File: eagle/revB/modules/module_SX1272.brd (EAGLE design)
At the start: 24.1 x 32.8 mm, 18 parts, among them X1 734120110

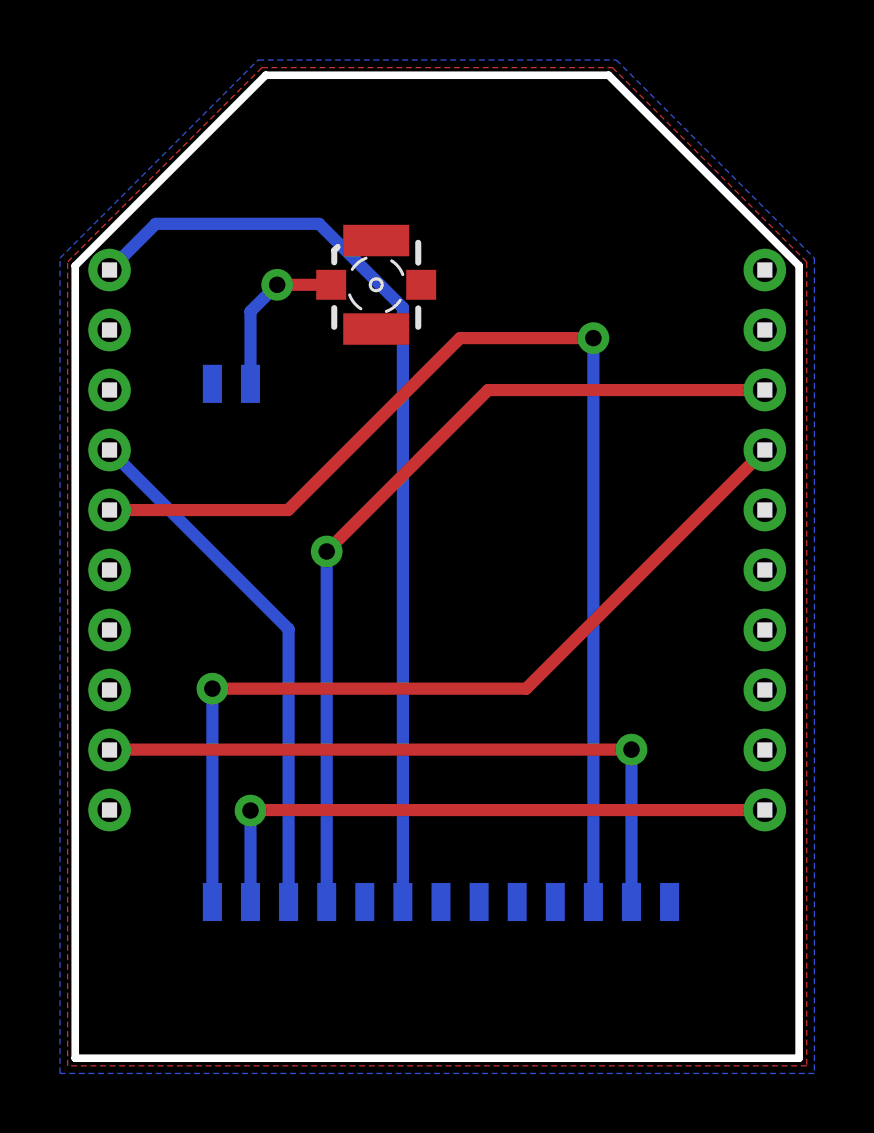
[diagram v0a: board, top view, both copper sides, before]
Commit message: Updated SX1272 layout
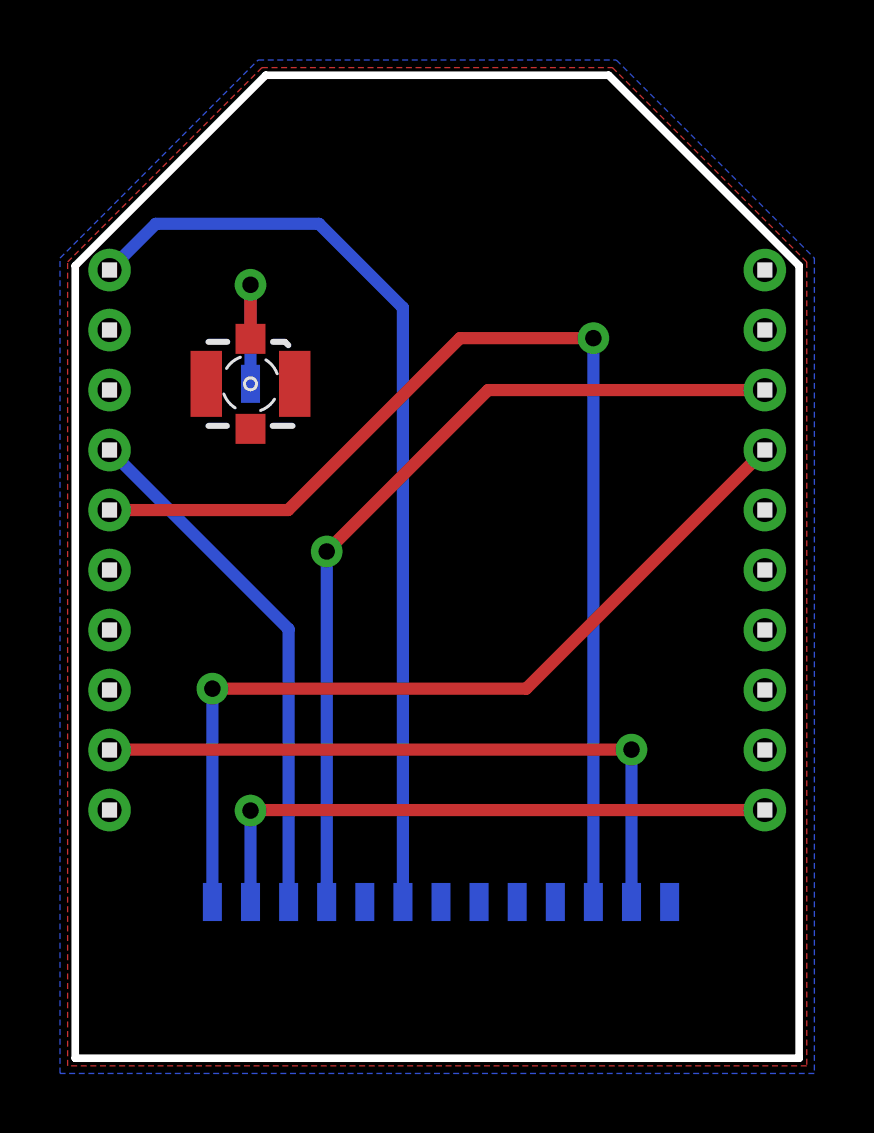
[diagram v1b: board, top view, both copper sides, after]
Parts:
- moved X1 5.34 mm to (5.97, 22.6), turned to 180 degrees
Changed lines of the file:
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@@
 <text x="20.282003125" y="4.17799375" size="0.6096" layer="126" font="vector" ratio="15" rot="MR270">RESET</text>
 <text x="8.852003125" y="4.17799375" size="0.6096" layer="126" font="vector" ratio="15" rot="MR270">SCK</text>
+<text x="12.065" y="26.162" size="1.524" layer="125" font="vector" ratio="15" align="center">SX1272</text>
 </plain>
 <attributes>
@@
 <element name="LEFT1" library="headers(2mm)" package="1X10" value="1X10" x="1.27" y="17.399" rot="R270"/>
 <element name="RIGHT1" library="headers(2mm)" package="1X10" value="1X10" x="23.114" y="17.399" rot="R270"/>
-<element name="X1" library="con-coax" package="734120110" value="734120110" x="10.16" y="25.908" smashed="yes" rot="R270"/>
+<element name="X1" library="con-coax" package="734120110" value="734120110" x="5.969" y="22.606" smashed="yes" rot="R180"/>
 <element name="SCK" library="wirepad" package="SMD0,65-1,27" value="" x="8.509" y="5.334" smashed="yes" rot="MR180">
 <attribute name="NAME" x="8.852" y="4.178" size="0.6096" layer="26" font="vector" ratio="12" rot="MR270"/>
@@
 <contactref element="X1" pad="1"/>
 <contactref element="ANT" pad="1"/>
-<wire x1="5.969" y1="22.606" x2="5.969" y2="25.019" width="0.4064" layer="16"/>
-<wire x1="5.969" y1="25.019" x2="6.858" y2="25.908" width="0.4064" layer="16"/>
-<via x="6.858" y="25.908" extent="1-16" drill="0.55"/>
-<wire x1="6.858" y1="25.908" x2="8.66" y2="25.908" width="0.4064" layer="1"/>
+<wire x1="5.969" y1="22.606" x2="5.969" y2="25.908" width="0.4064" layer="16"/>
+<via x="5.969" y="25.908" extent="1-16" drill="0.55"/>
+<wire x1="5.969" y1="25.908" x2="5.969" y2="24.106" width="0.4064" layer="1"/>
 </signal>
 <signal name="INT1">
